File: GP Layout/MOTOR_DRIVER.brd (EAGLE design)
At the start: 91.4 x 97.5 mm, 46 parts, among them U2 CSD18502KCS_KCS_3, U3 MIC4604YM, U4 CSD18502KCS_KCS_3, U5 CSD18502KCS_KCS_3, U6 MIC4604YM, U7 ATMEGA328P_TQFP, Y1 16MHz

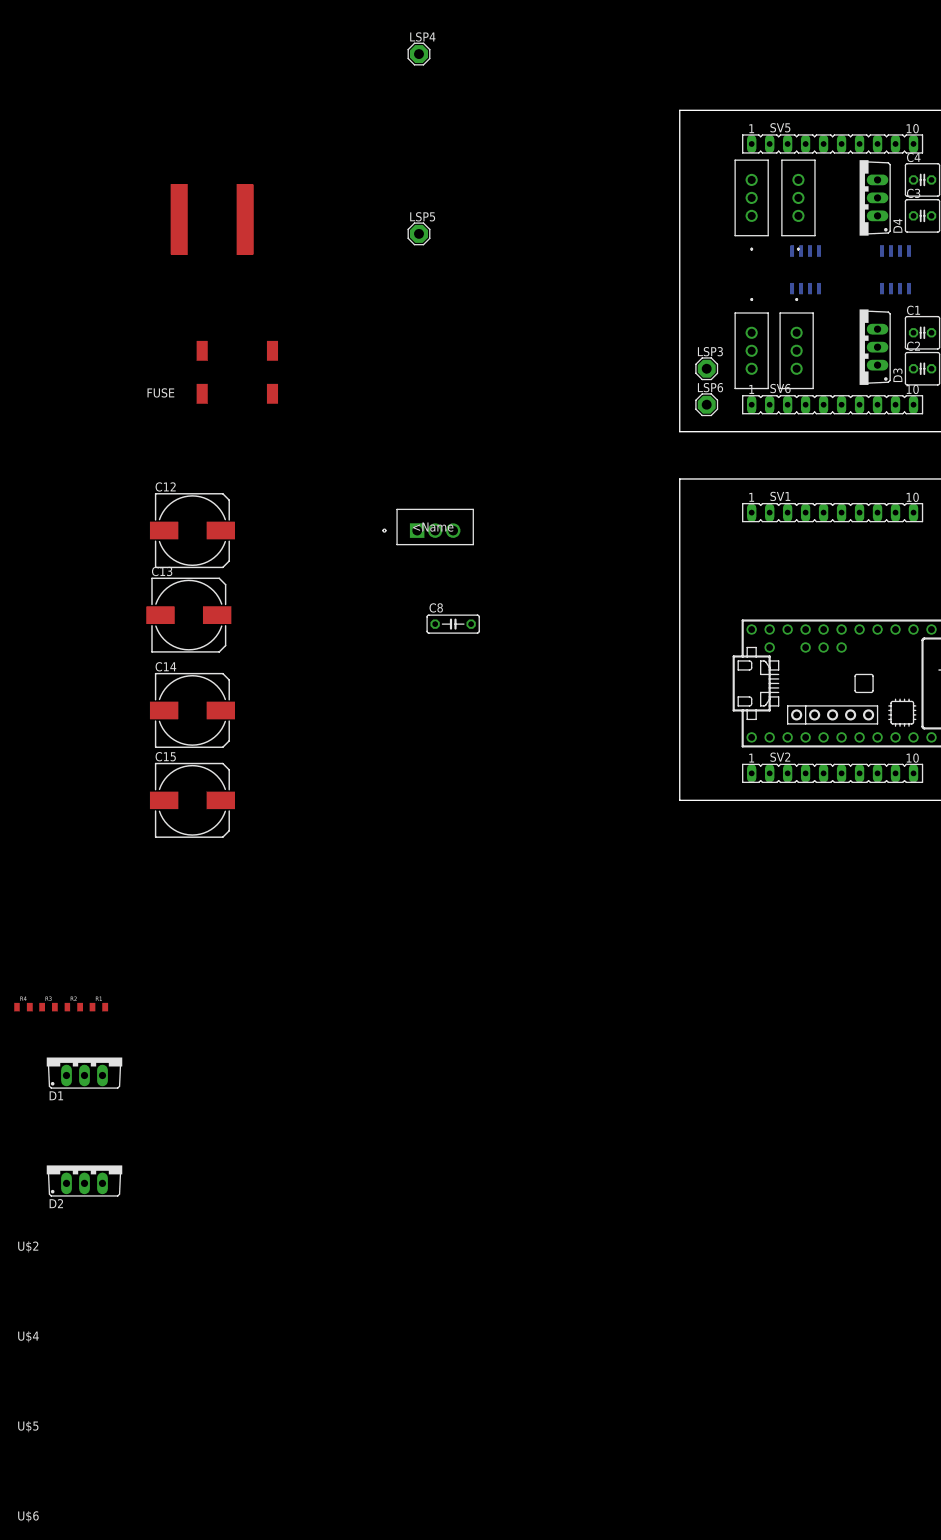
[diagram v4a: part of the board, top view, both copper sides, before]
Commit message: modified footprint for MOS to have name and indicate orientation
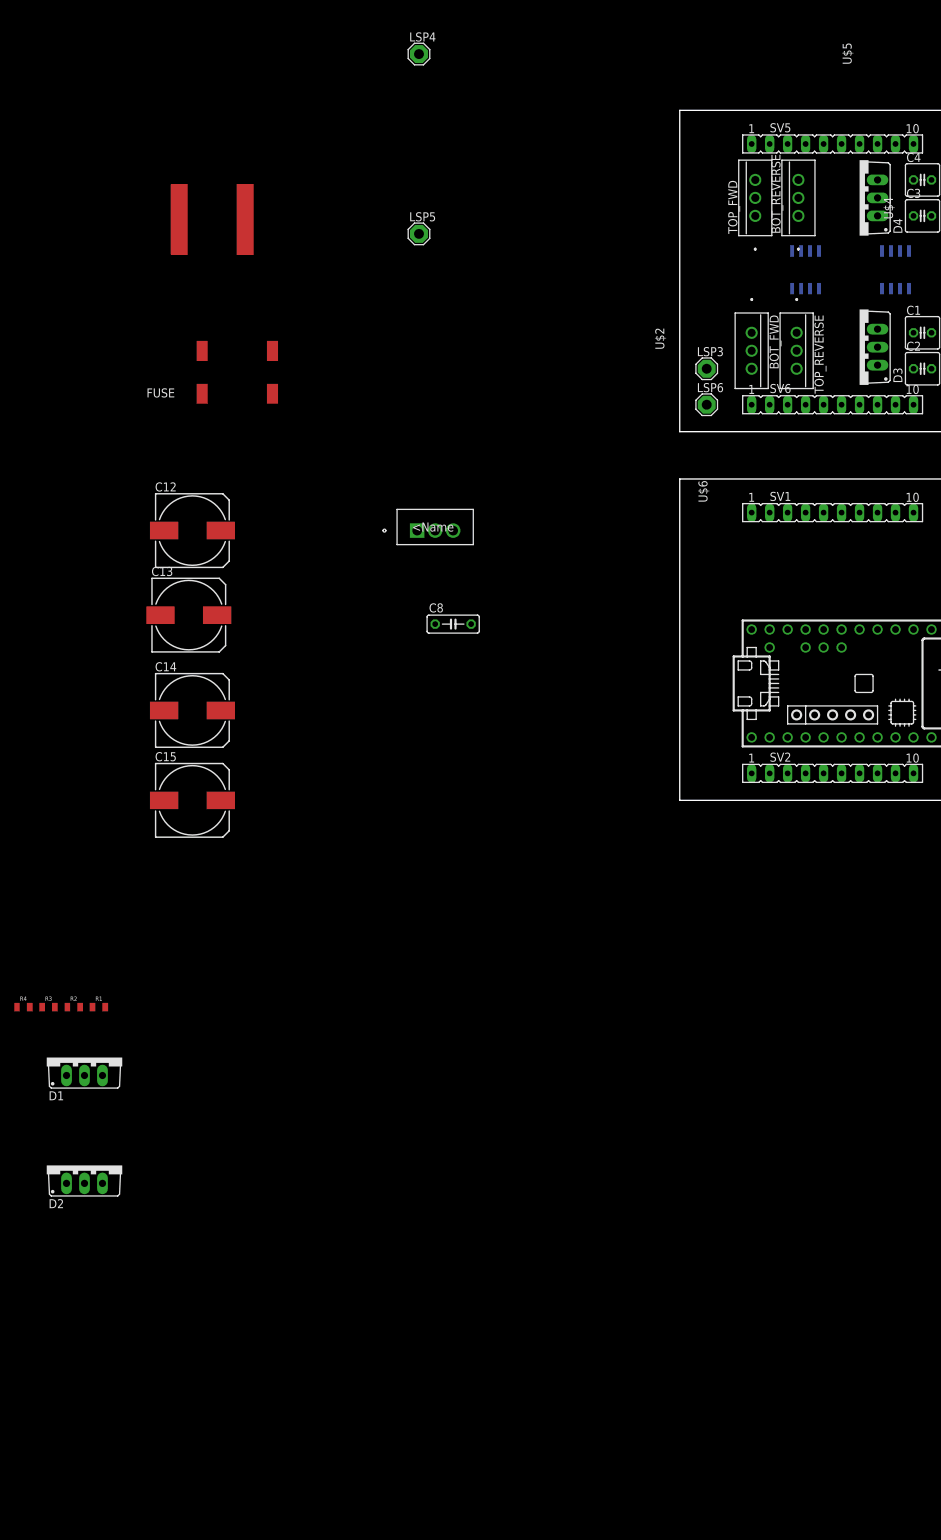
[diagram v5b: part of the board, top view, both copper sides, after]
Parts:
- moved U$5 202.9 mm to (13.2, 85.3), turned to 270 degrees
- moved U$6 195.0 mm to (13.7, 63.8), turned to 90 degrees
- moved U$2 177.5 mm to (7.62, 85.3), turned to 90 degrees
- moved U$4 175.1 mm to (19.1, 63.5), turned to 270 degrees
- moved TOP_FWD 0.51 mm to (10.7, 87.6)
- renumbered U2 to BOT_REVERSE, U4 to TOP_REVERSE, U5 to BOT_FWD
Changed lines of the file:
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@@
 <element name="S1" library="smd-special" package="SMS-006" value="SWS006" x="83.82" y="16.51" rot="R90"/>
 <element name="U$1" library="Teensy356" package="TEENSY_3.5/3.6_BASIC" value="TEENSY_3.5/3.6_BASIC" x="38.1" y="16.51"/>
-<element name="TOP_FWD" library="CSD18502KCS" package="KCS3" value="CSD18502KCS_KCS_3" x="10.16" y="87.63" rot="R90">
-<attribute name="MANUFACTURER_PART_NUMBER" value="csd18502kcs_kcs_3" x="10.16" y="87.63" size="1.778" layer="27" rot="R90" display="off"/>
-<attribute name="VENDOR" value="TEXAS INSTRUMENTS" x="10.16" y="87.63" size="1.778" layer="27" rot="R90" display="off"/>
-</element>
-<element name="U2" library="CSD18502KCS" package="KCS3" value="CSD18502KCS_KCS_3" x="16.764" y="87.63" rot="R90">
+<element name="TOP_FWD" library="CSD18502KCS" package="KCS3" value="CSD18502KCS_KCS_3" x="10.668" y="87.63" rot="R90">
+<attribute name="MANUFACTURER_PART_NUMBER" value="csd18502kcs_kcs_3" x="10.668" y="87.63" size="1.778" layer="27" rot="R90" display="off"/>
+<attribute name="VENDOR" value="TEXAS INSTRUMENTS" x="10.668" y="87.63" size="1.778" layer="27" rot="R90" display="off"/>
+</element>
+<element name="BOT_REVERSE" library="CSD18502KCS" package="KCS3" value="CSD18502KCS_KCS_3" x="16.764" y="87.63" rot="R90">
 <attribute name="MANUFACTURER_PART_NUMBER" value="csd18502kcs_kcs_3" x="16.764" y="87.63" size="1.778" layer="27" rot="R90" display="off"/>
 <attribute name="VENDOR" value="TEXAS INSTRUMENTS" x="16.764" y="87.63" size="1.778" layer="27" rot="R90" display="off"/>
@@
 <attribute name="VENDOR" value="Microchip" x="17.78" y="74.93" size="1.778" layer="28" rot="MR270" display="off"/>
 </element>
-<element name="U4" library="CSD18502KCS" package="KCS3" value="CSD18502KCS_KCS_3" x="16.51" y="60.96" rot="R270">
+<element name="TOP_REVERSE" library="CSD18502KCS" package="KCS3" value="CSD18502KCS_KCS_3" x="16.51" y="60.96" rot="R270">
 <attribute name="MANUFACTURER_PART_NUMBER" value="csd18502kcs_kcs_3" x="16.51" y="60.96" size="1.778" layer="27" rot="R270" display="off"/>
 <attribute name="VENDOR" value="TEXAS INSTRUMENTS" x="16.51" y="60.96" size="1.778" layer="27" rot="R270" display="off"/>
 </element>
-<element name="U5" library="CSD18502KCS" package="KCS3" value="CSD18502KCS_KCS_3" x="10.16" y="60.96" rot="R270">
+<element name="BOT_FWD" library="CSD18502KCS" package="KCS3" value="CSD18502KCS_KCS_3" x="10.16" y="60.96" rot="R270">
 <attribute name="MANUFACTURER_PART_NUMBER" value="csd18502kcs_kcs_3" x="10.16" y="60.96" size="1.778" layer="27" rot="R270" display="off"/>
 <attribute name="VENDOR" value="TEXAS INSTRUMENTS" x="10.16" y="60.96" size="1.778" layer="27" rot="R270" display="off"/>
@@
 <element name="D1" library="diode" package="TO220ABS" value="BYV32" x="-84.074" y="-36.322"/>
 <element name="D2" library="diode" package="TO220ABS" value="BYV32" x="-84.074" y="-51.562"/>
-<element name="U$2" library="heatsink" package="HEATSINK" value="HEATSINK" x="-71.882" y="-73.406"/>
-<element name="U$4" library="heatsink" package="HEATSINK" value="HEATSINK" x="-71.882" y="-86.106"/>
-<element name="U$5" library="heatsink" package="HEATSINK" value="HEATSINK" x="-71.882" y="-98.806"/>
-<element name="U$6" library="heatsink" package="HEATSINK" value="HEATSINK" x="-71.882" y="-111.506"/>
+<element name="U$2" library="heatsink" package="HEATSINK" value="HEATSINK" x="7.62" y="85.344" rot="R90"/>
+<element name="U$4" library="heatsink" package="HEATSINK" value="HEATSINK" x="19.05" y="63.5" rot="R270"/>
+<element name="U$5" library="heatsink" package="HEATSINK" value="HEATSINK" x="13.208" y="85.344" rot="R270"/>
+<element name="U$6" library="heatsink" package="HEATSINK" value="HEATSINK" x="13.716" y="63.754" rot="R90"/>
 </elements>
 <signals>
@@
 <signal name="N$2">
 <contactref element="U3" pad="8"/>
-<contactref element="U2" pad="1"/>
+<contactref element="BOT_REVERSE" pad="1"/>
 <wire x1="15.875" y1="72.2757" x2="16.764" y2="82.55" width="0" layer="19" extent="16-16"/>
 </signal>
@@
 <contactref element="TOP_FWD" pad="1"/>
 <contactref element="U3" pad="3"/>
-<wire x1="10.16" y1="82.55" x2="18.415" y2="77.5843" width="0" layer="19" extent="16-16"/>
+<wire x1="10.668" y1="82.55" x2="18.415" y2="77.5843" width="0" layer="19" extent="16-16"/>
 </signal>
 <signal name="N$4">
@@
 <signal name="N$9">
 <contactref element="U6" pad="8"/>
-<contactref element="U5" pad="1"/>
+<contactref element="BOT_FWD" pad="1"/>
 <wire x1="10.16" y1="66.04" x2="28.575" y2="72.2757" width="0" layer="19" extent="16-16"/>
 </signal>
 <signal name="N$10">
-<contactref element="U4" pad="1"/>
+<contactref element="TOP_REVERSE" pad="1"/>
 <contactref element="U6" pad="3"/>
 <wire x1="16.51" y1="66.04" x2="31.115" y2="77.5843" width="0" layer="19" extent="16-16"/>
@@
 <contactref element="TOP_FWD" pad="2"/>
 <contactref element="U3" pad="1"/>
-<contactref element="U4" pad="2"/>
+<contactref element="TOP_REVERSE" pad="2"/>
 <contactref element="U6" pad="1"/>
 <contactref element="BIG_SWITCH" pad="GND"/>
 <wire x1="16.51" y1="63.5" x2="-61.39" y2="82.042" width="0" layer="19" extent="1-1"/>
 <wire x1="15.875" y1="77.5843" x2="16.51" y2="63.5" width="0" layer="19" extent="16-16"/>
-<wire x1="10.16" y1="85.09" x2="15.875" y2="77.5843" width="0" layer="19" extent="16-16"/>
-<wire x1="10.16" y1="92.71" x2="10.16" y2="85.09" width="0" layer="19" extent="1-1"/>
+<wire x1="10.668" y1="85.09" x2="15.875" y2="77.5843" width="0" layer="19" extent="16-16"/>
+<wire x1="10.16" y1="92.71" x2="10.668" y2="85.09" width="0" layer="19" extent="1-1"/>
 <wire x1="28.575" y1="77.5843" x2="15.875" y2="77.5843" width="0" layer="19" extent="16-16"/>
 <wire x1="27.94" y1="82.55" x2="28.575" y2="77.5843" width="0" layer="19" extent="16-16"/>
 <wire x1="27.94" y1="87.63" x2="27.94" y2="82.55" width="0" layer="19" extent="1-1"/>
-<wire x1="27.94" y1="61.468" x2="10.16" y2="85.09" width="0" layer="19" extent="1-1"/>
+<wire x1="27.94" y1="61.468" x2="10.668" y2="85.09" width="0" layer="19" extent="1-1"/>
 <wire x1="27.94" y1="66.548" x2="27.94" y2="61.468" width="0" layer="19" extent="1-1"/>
 </signal>
@@
 <signal name="GND_TOP">
 <contactref element="SV5" pad="10"/>
-<contactref element="U2" pad="3"/>
+<contactref element="BOT_REVERSE" pad="3"/>
 <contactref element="U3" pad="7"/>
-<contactref element="U5" pad="3"/>
+<contactref element="BOT_FWD" pad="3"/>
 <contactref element="U6" pad="7"/>
 <contactref element="C12" pad="-"/>
@@
 <signal name="MOTOR_HIGH_TOP">
 <contactref element="TOP_FWD" pad="3"/>
-<contactref element="U2" pad="2"/>
+<contactref element="BOT_REVERSE" pad="2"/>
 <contactref element="LSP3" pad="MP"/>
 <contactref element="SV6" pad="3"/>
-<wire x1="10.16" y1="87.63" x2="16.764" y2="85.09" width="0" layer="19" extent="1-1"/>
+<wire x1="10.668" y1="87.63" x2="16.764" y2="85.09" width="0" layer="19" extent="1-1"/>
 <wire x1="3.81" y1="60.96" x2="16.764" y2="85.09" width="0" layer="19" extent="1-1"/>
 <wire x1="15.24" y1="55.88" x2="3.81" y2="60.96" width="0" layer="19" extent="1-1"/>
 </signal>
 <signal name="MOTOR_LOW_TOP">
-<contactref element="U4" pad="3"/>
-<contactref element="U5" pad="2"/>
+<contactref element="TOP_REVERSE" pad="3"/>
+<contactref element="BOT_FWD" pad="2"/>
 <contactref element="LSP6" pad="MP"/>
 <contactref element="SV6" pad="4"/>

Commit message: Changed battery sense resistances
Input impedance might be too high for the Teensy ADC
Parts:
- R1: value 2.8M -> 9090
- R2: value 1.62M -> 4750
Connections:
- net 5V: now also SV1.8
- net GND: now also SV1.10
- net SERVO: now also SV1.9
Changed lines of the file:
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@@
 <?xml version="1.0" encoding="utf-8"?>
 <!DOCTYPE eagle SYSTEM "eagle.dtd">
-<eagle version="8.0.1">
+<eagle version="8.0.0">
 <drawing>
 <settings>
@@
 <element name="FUSE" library="minifuse" package="FUSEHOLDER3588" value="" x="-62.484" y="60.452" rot="R180"/>
 <element name="BIG_SWITCH" library="bigswitch" package="BIGSWITCH" value="" x="-66.04" y="82.042"/>
-<element name="R1" library="SparkFun-Resistors" package="0805" value="2.8M" x="-82.042" y="-29.21">
+<element name="R1" library="SparkFun-Resistors" package="0805" value="9090" x="-82.042" y="-29.21">
 <attribute name="PROD_ID" value="RES-11622" x="-82.042" y="-29.21" size="1.778" layer="27" display="off"/>
 </element>
-<element name="R2" library="SparkFun-Resistors" package="0805" value="1.62M" x="-85.598" y="-29.21">
+<element name="R2" library="SparkFun-Resistors" package="0805" value="4750" x="-85.598" y="-29.21">
 <attribute name="PROD_ID" value="RES-11622" x="-85.598" y="-29.21" size="1.778" layer="27" display="off"/>
 </element>
@@
 <contactref element="SV3" pad="2"/>
 <contactref element="R2" pad="1"/>
-<wire x1="-37.084" y1="38.1" x2="-86.498" y2="-29.21" width="0" layer="19" extent="1-1"/>
-<wire x1="-29.464" y1="24.892" x2="-37.084" y2="38.1" width="0" layer="19" extent="1-1"/>
+<contactref element="SV1" pad="10"/>
+<wire x1="-29.464" y1="24.892" x2="-86.498" y2="-29.21" width="0" layer="19" extent="1-1"/>
+<wire x1="-37.084" y1="38.1" x2="-29.464" y2="24.892" width="0" layer="19" extent="1-1"/>
 <wire x1="12.7" y1="24.13" x2="-29.464" y2="24.892" width="0" layer="19" extent="1-1"/>
 <wire x1="10.16" y1="8.89" x2="12.7" y2="24.13" width="0" layer="19" extent="1-1"/>
-<wire x1="45.72" y1="24.13" x2="12.7" y2="24.13" width="0" layer="19" extent="1-1"/>
+<wire x1="33.02" y1="40.64" x2="12.7" y2="24.13" width="0" layer="19" extent="1-1"/>
+<wire x1="45.72" y1="24.13" x2="33.02" y2="40.64" width="0" layer="19" extent="1-1"/>
 <wire x1="53.34" y1="21.59" x2="45.72" y2="24.13" width="0" layer="19" extent="1-1"/>
 <wire x1="59.2074" y1="17.71" x2="53.34" y2="21.59" width="0" layer="19" extent="1-1"/>
@@
 <signal name="SERVO">
 <contactref element="U$1" pad="20/A6"/>
+<contactref element="SV1" pad="9"/>
+<wire x1="25.4" y1="24.13" x2="30.48" y2="40.64" width="0" layer="19" extent="1-1"/>
 </signal>
 <signal name="BLT_RX">
@@
 <contactref element="C8" pad="1"/>
 <contactref element="SV3" pad="6"/>
+<contactref element="SV1" pad="8"/>
 <wire x1="66.04" y1="40.64" x2="78.74" y2="38.1" width="0" layer="19" extent="1-1"/>
 <wire x1="63.5" y1="38.1" x2="66.04" y2="40.64" width="0" layer="19" extent="1-1"/>
 <wire x1="79.3242" y1="22.86" x2="78.74" y2="38.1" width="0" layer="19" extent="1-1"/>
-<wire x1="-34.544" y1="24.892" x2="63.5" y2="38.1" width="0" layer="19" extent="1-1"/>
-<wire x1="-34.544" y1="38.1" x2="-34.544" y2="24.892" width="0" layer="19" extent="1-1"/>
+<wire x1="27.94" y1="40.64" x2="63.5" y2="38.1" width="0" layer="19" extent="1-1"/>
+<wire x1="-34.544" y1="38.1" x2="27.94" y2="40.64" width="0" layer="19" extent="1-1"/>
+<wire x1="-34.544" y1="24.892" x2="-34.544" y2="38.1" width="0" layer="19" extent="1-1"/>
 </signal>
 <signal name="3_3V">

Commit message: added motor inputs for full bridge
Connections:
- net HI renamed HI1
- net LI renamed LI1
- new net HI1_TOP: SV6.1, U3.5
- new net HI2: SV2.3, U$1.5
- new net HI2_TOP: SV6.3
- new net LI1_TOP: SV6.2, U3.6
- new net LI2: SV2.4, U$1.6
- new net LI2_TOP: SV6.4
- net HI_TOP: no longer SV6.1, U3.5
- net LI_TOP: no longer SV6.2, U3.6
- net MOTOR_HIGH: now also SV2.5; no longer SV2.3
- net MOTOR_HIGH_TOP: no longer SV6.3
- net MOTOR_LOW: now also SV2.6; no longer SV2.4
- net MOTOR_LOW_TOP: now also SV6.5, SV6.6; no longer SV6.4
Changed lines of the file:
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@@
 <?xml version="1.0" encoding="utf-8"?>
 <!DOCTYPE eagle SYSTEM "eagle.dtd">
-<eagle version="8.0.0">
+<eagle version="8.0.1">
 <drawing>
 <settings>
@@
 <signal name="MOTOR_HIGH">
 <contactref element="R3" pad="2"/>
-<contactref element="SV2" pad="3"/>
-<wire x1="15.24" y1="3.81" x2="-88.254" y2="-29.21" width="0" layer="19" extent="1-1"/>
+<contactref element="SV2" pad="5"/>
+<wire x1="20.32" y1="3.81" x2="-88.254" y2="-29.21" width="0" layer="19" extent="1-1"/>
 </signal>
 <signal name="N$2">
@@
 <contactref element="D2" pad="A2"/>
 <contactref element="D2" pad="A1"/>
-<contactref element="SV2" pad="4"/>
+<contactref element="SV2" pad="6"/>
 <wire x1="-81.534" y1="-54.102" x2="-86.614" y2="-54.102" width="0" layer="19" extent="1-1"/>
 <wire x1="-93.61" y1="-29.21" x2="-86.614" y2="-54.102" width="0" layer="19" extent="1-1"/>
-<wire x1="17.78" y1="3.81" x2="-81.534" y2="-54.102" width="0" layer="19" extent="1-1"/>
+<wire x1="22.86" y1="3.81" x2="-81.534" y2="-54.102" width="0" layer="19" extent="1-1"/>
 </signal>
 <signal name="N$9">
@@
 <wire x1="73.66" y1="38.1" x2="71.12" y2="38.1" width="0" layer="19" extent="1-1"/>
 </signal>
-<signal name="LI">
-<contactref element="U$1" pad="4/CANRX"/>
-<contactref element="SV2" pad="2"/>
-<wire x1="12.7" y1="3.81" x2="22.86" y2="8.89" width="0" layer="19" extent="1-1"/>
-</signal>
-<signal name="HI">
-<contactref element="U$1" pad="3/CANTX"/>
-<contactref element="SV2" pad="1"/>
-<wire x1="10.16" y1="3.81" x2="20.32" y2="8.89" width="0" layer="19" extent="1-1"/>
-</signal>
 <signal name="N$6">
 <contactref element="U7" pad="7"/>
@@
 </signal>
 <signal name="LI_TOP">
-<contactref element="U3" pad="6"/>
 <contactref element="U6" pad="5"/>
-<contactref element="SV6" pad="2"/>
-<wire x1="18.415" y1="72.2757" x2="32.385" y2="72.2757" width="0" layer="19" extent="16-16"/>
-<wire x1="12.7" y1="55.88" x2="18.415" y2="72.2757" width="0" layer="19" extent="16-16"/>
 </signal>
 <signal name="HI_TOP">
-<contactref element="U3" pad="5"/>
 <contactref element="U6" pad="6"/>
-<contactref element="SV6" pad="1"/>
-<wire x1="19.685" y1="72.2757" x2="31.115" y2="72.2757" width="0" layer="19" extent="16-16"/>
-<wire x1="10.16" y1="55.88" x2="19.685" y2="72.2757" width="0" layer="19" extent="16-16"/>
 </signal>
 <signal name="GND_TOP">
@@
 <contactref element="BOT_REVERSE" pad="2"/>
 <contactref element="LSP3" pad="MP"/>
-<contactref element="SV6" pad="3"/>
 <wire x1="10.668" y1="87.63" x2="16.764" y2="85.09" width="0" layer="19" extent="1-1"/>
 <wire x1="3.81" y1="60.96" x2="16.764" y2="85.09" width="0" layer="19" extent="1-1"/>
-<wire x1="15.24" y1="55.88" x2="3.81" y2="60.96" width="0" layer="19" extent="1-1"/>
 </signal>
 <signal name="MOTOR_LOW_TOP">
@@
 <contactref element="BOT_FWD" pad="2"/>
 <contactref element="LSP6" pad="MP"/>
-<contactref element="SV6" pad="4"/>
-<wire x1="17.78" y1="55.88" x2="16.51" y2="60.96" width="0" layer="19" extent="1-1"/>
+<contactref element="SV6" pad="6"/>
+<contactref element="SV6" pad="5"/>
+<wire x1="20.32" y1="55.88" x2="22.86" y2="55.88" width="0" layer="19" extent="1-1"/>
+<wire x1="16.51" y1="60.96" x2="20.32" y2="55.88" width="0" layer="19" extent="1-1"/>
 <wire x1="10.16" y1="63.5" x2="16.51" y2="60.96" width="0" layer="19" extent="1-1"/>
 <wire x1="3.81" y1="55.88" x2="10.16" y2="63.5" width="0" layer="19" extent="1-1"/>
 </signal>
+<signal name="HI1">
+<contactref element="U$1" pad="3/CANTX"/>
+<contactref element="SV2" pad="1"/>
+<wire x1="10.16" y1="3.81" x2="20.32" y2="8.89" width="0" layer="19" extent="1-1"/>
+</signal>
+<signal name="LI1">
+<contactref element="U$1" pad="4/CANRX"/>
+<contactref element="SV2" pad="2"/>
+<wire x1="12.7" y1="3.81" x2="22.86" y2="8.89" width="0" layer="19" extent="1-1"/>
+</signal>
+<signal name="LI1_TOP">
+<contactref element="SV6" pad="2"/>
+<contactref element="U3" pad="6"/>
+<wire x1="12.7" y1="55.88" x2="18.415" y2="72.2757" width="0" layer="19" extent="16-16"/>
+</signal>
+<signal name="HI1_TOP">
+<contactref element="SV6" pad="1"/>
+<contactref element="U3" pad="5"/>
+<wire x1="10.16" y1="55.88" x2="19.685" y2="72.2757" width="0" layer="19" extent="16-16"/>
+</signal>
+<signal name="HI2">
+<contactref element="U$1" pad="5"/>
+<contactref element="SV2" pad="3"/>
+<wire x1="15.24" y1="3.81" x2="25.4" y2="8.89" width="0" layer="19" extent="1-1"/>
+</signal>
+<signal name="LI2">
+<contactref element="U$1" pad="6"/>
+<contactref element="SV2" pad="4"/>
+<wire x1="17.78" y1="3.81" x2="27.94" y2="8.89" width="0" layer="19" extent="1-1"/>
+</signal>
+<signal name="HI2_TOP">
+<contactref element="SV6" pad="3"/>
+</signal>
+<signal name="LI2_TOP">
+<contactref element="SV6" pad="4"/>
+</signal>
 </signals>
